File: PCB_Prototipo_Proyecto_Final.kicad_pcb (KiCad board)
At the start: 2 copper layers, 165.1 x 154.9 mm, 107 parts, among them IC1 MCP6486T-E_OT, J1 VIN, J10 Terminal_Sensores_Nivel, J11 Terminal_Sensor_Flujo, J12 Rele_4, J13 Rele_7, J14 Rele_1, J15 Rele_5, J16 Rele_2, J17 Rele_3, J18 Rele_6, J2 Conn_01x15, J3 Conn_01x15, J4 Terminal_Sensor_pH, J5 Terminal_Sensor_Temp_Sumerg, J6 Terminal_Sensor_TDS, J7 Terminal_Sensor_Temp_Sumerg, J8 Terminal_Sensor_Iluminacion, J9 Terminal_Sensor_Temp_y_Hum, K1 SRD-05VDC-SL-C, K2 SRD-05VDC-SL-C, K3 SRD-05VDC-SL-C, K4 SRD-05VDC-SL-C, K5 SRD-05VDC-SL-C, K6 SRD-05VDC-SL-C, K7 SRD-05VDC-SL-C, Q1 PMBT3904,235, Q2 PMBT3904,235, Q3 PMBT3904,235, Q4 PMBT3904,235, Q5 PMBT3904,235, Q6 PMBT3904,235, Q7 PMBT3904,235, U1 LM2596S-5, U2 LM1117-3.3, U3 NXB0108PW-Q100J, U4 MCP23008-xSS

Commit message: Cambios en SCH y PCB.
Se cambio el adaptador de nivel 5-3,3V por un circuito con MOSFET 2N7002, dado que ya no hay stock del NXB. Se modificó el footprint del expansor I/O por uno thorugh-hole.
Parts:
- removed the C19 at (179.2, 156.3)
- removed the C20 at (179.2, 159.3)
- removed C21: 10 uF, 10V, Capacitor_SMD:C_0805_2012Metric
- removed C22: 100 nF, 50V, Capacitor_SMD:C_0805_2012Metric
- removed U4: MCP23008-xSS, Package_SO:SSOP-20_5.3x7.2mm_P0.65mm
- added Q1: 2N7002, Package_TO_SOT_SMD:SOT-23, F.Cu at (163.2, 122.3)
- added Q2: 2N7002, Package_TO_SOT_SMD:SOT-23, F.Cu at (153.3, 186.1)
- added Q3: 2N7002, Package_TO_SOT_SMD:SOT-23, F.Cu at (168.2, 186.0)
- added Q4: 2N7002, Package_TO_SOT_SMD:SOT-23, F.Cu at (183.2, 185.8)
- added Q5: 2N7002, Package_TO_SOT_SMD:SOT-23, F.Cu at (198.3, 185.9)
- added Q6: 2N7002, Package_TO_SOT_SMD:SOT-23, F.Cu at (213.6, 186.1)
- added Q7: 2N7002, Package_TO_SOT_SMD:SOT-23, F.Cu at (161.7, 161.9)
- added Q8: 2N7002, Package_TO_SOT_SMD:SOT-23, F.Cu at (161.2, 143.3)
- added R25: 10K, 1/2W, Resistor_SMD:R_0805_2012Metric, F.Cu at (156.8, 122.4)
- added R26: 10K, 1/2W, Resistor_SMD:R_0805_2012Metric, F.Cu at (163.2, 117.2)
- added R27: 10K, 1/2W, Resistor_SMD:R_0805_2012Metric, F.Cu at (153.3, 191.8)
- added R28: 10K, 1/2W, Resistor_SMD:R_0805_2012Metric, F.Cu at (153.1, 181.0)
- added R29: 10K, 1/2W, Resistor_SMD:R_0805_2012Metric, F.Cu at (168.3, 191.8)
- added R30: 10K, 1/2W, Resistor_SMD:R_0805_2012Metric, F.Cu at (168.2, 180.8)
- added R31: 10K, 1/2W, Resistor_SMD:R_0805_2012Metric, F.Cu at (183.2, 191.6)
- added R32: 10K, 1/2W, Resistor_SMD:R_0805_2012Metric, F.Cu at (183.1, 180.6)
- added R33: 10K, 1/2W, Resistor_SMD:R_0805_2012Metric, F.Cu at (198.2, 191.6)
- added R34: 10K, 1/2W, Resistor_SMD:R_0805_2012Metric, F.Cu at (198.2, 180.4)
- added R35: 10K, 1/2W, Resistor_SMD:R_0805_2012Metric, F.Cu at (213.4, 191.5)
- added R36: 10K, 1/2W, Resistor_SMD:R_0805_2012Metric, F.Cu at (213.6, 180.3)
- added R37: 10K, 1/2W, Resistor_SMD:R_0805_2012Metric, F.Cu at (156.0, 160.9)
- added R38: 10K, 1/2W, Resistor_SMD:R_0805_2012Metric, F.Cu at (161.8, 157.4)
- added R39: 10K, 1/2W, Resistor_SMD:R_0805_2012Metric, F.Cu at (155.6, 143.2)
- added R40: 10K, 1/2W, Resistor_SMD:R_0805_2012Metric, F.Cu at (161.2, 139.0)
- J5: value Terminal_Sensor_Temp_Sumerg -> Terminal_Sensor_CO2
- U3: value NXB0108PW-Q100J -> MCP23008-xP; footprint Package_SO:TSSOP-20_4.4x6.5mm_P0.65mm -> Package_DIP:DIP-18_W7.62mm
- moved R7 336.8 mm to (158.3, 183.3), turned to 90 degrees
- moved R23 332.4 mm to (155.7, 148.5)
- moved C1 329.2 mm to (159.1, 187.9)
- moved R6 321.2 mm to (158.2, 191.8), turned to 90 degrees
- moved R16 320.3 mm to (156.1, 166.3)
- moved C2 319.0 mm to (174.0, 187.4)
- moved R10 318.5 mm to (188.2, 191.7), turned to 90 degrees
- moved R9 316.7 mm to (173.0, 183.1), turned to 90 degrees
- moved C6 315.4 mm to (161.7, 167.3), turned to -90 degrees
- moved C11 315.0 mm to (161.2, 149.4), turned to -90 degrees
- moved R8 307.2 mm to (173.1, 191.7), turned to 90 degrees
- moved R11 301.2 mm to (188.2, 183.0), turned to 90 degrees
- moved C3 293.4 mm to (189.1, 187.2)
- moved R12 287.9 mm to (203.3, 191.6), turned to 90 degrees
- moved C4 284.6 mm to (204.3, 187.1)
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- renumbered C23 to C19, C24 to C20, Q2 to Q10, Q3 to Q11, Q4 to Q12, Q5 to Q13, Q6 to Q14, Q7 to Q15, Q1 to Q9, R25 to R41, R26 to R42, R27 to R43, R28 to R44, R29 to R45, R30 to R46, R31 to R47, R32 to R48, R33 to R49
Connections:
- J2 pad 11: /Microcontrolador/SensorNivel_2 -> /Microcontrolador/SensorNivel_4
- J2 pad 12: /Microcontrolador/SensorNivel_1 -> /Microcontrolador/SensorNivel_5
- J2 pad 13: /Microcontrolador/NXB0108_OE -> unconnected-(J2-Pad13)
- J2 pad 3: /Entradas/TDS_Analog -> unconnected-(J2-Pad3)
- J2 pad 4: /Entradas/Ilum_Analog -> unconnected-(J2-Pad4)
- J2 pad 8: /Microcontrolador/SensorNivel_5 -> /Microcontrolador/SensorNivel_1
- J2 pad 9: /Microcontrolador/SensorNivel_4 -> /Microcontrolador/SensorNivel_2
- J3 pad 12: unconnected-(J3-Pad12) -> /Entradas/TDS_Analog
- J3 pad 13: unconnected-(J3-Pad13) -> /Entradas/Ilum_Analog
- J3 pad 15: unconnected-(J3-Pad15) -> +3.3V
- U3 pad 1: /Microcontrolador/SensorFlujo -> /Microcontrolador/MCP23008_SCL
- U3 pad 10: /Microcontrolador/NXB0108_OE -> /Microcontrolador/Rele_7
- U3 pad 11: GND -> /Microcontrolador/Rele_6
- U3 pad 12: /Entradas/Trigger_pH -> /Microcontrolador/Rele_5
- U3 pad 13: /Entradas/Data_SensorNivel_1 -> /Microcontrolador/Rele_4
- U3 pad 14: /Entradas/Data_SensorNivel_2 -> /Microcontrolador/Rele_3
- U3 pad 15: /Entradas/Data_SensorNivel_3 -> /Microcontrolador/Rele_2
- U3 pad 16: /Entradas/Data_SensorNivel_4 -> /Microcontrolador/Rele_1
- U3 pad 17: /Entradas/Data_SensorNivel_5 -> /Microcontrolador/Trigger__pH
- U3 pad 18: /Entradas/Data_SensorCO2 -> +3.3V
- U3 pad 2: +3.3V -> /Microcontrolador/MCP23008_SDA
- U3 pad 3: /Microcontrolador/SensorCO2 -> GND
- U3 pad 4: /Microcontrolador/SensorNivel_5 -> GND
- U3 pad 5: /Microcontrolador/SensorNivel_4 -> GND
- U3 pad 6: /Microcontrolador/SensorNivel_3 -> /Microcontrolador/MCP23008_RESET
- U3 pad 7: /Microcontrolador/SensorNivel_2 -> unconnected-(U3-Pad7)
- U3 pad 8: /Microcontrolador/SensorNivel_1 -> unconnected-(U3-Pad8)
- U3 pad 9: /Microcontrolador/Trigger__pH -> GND

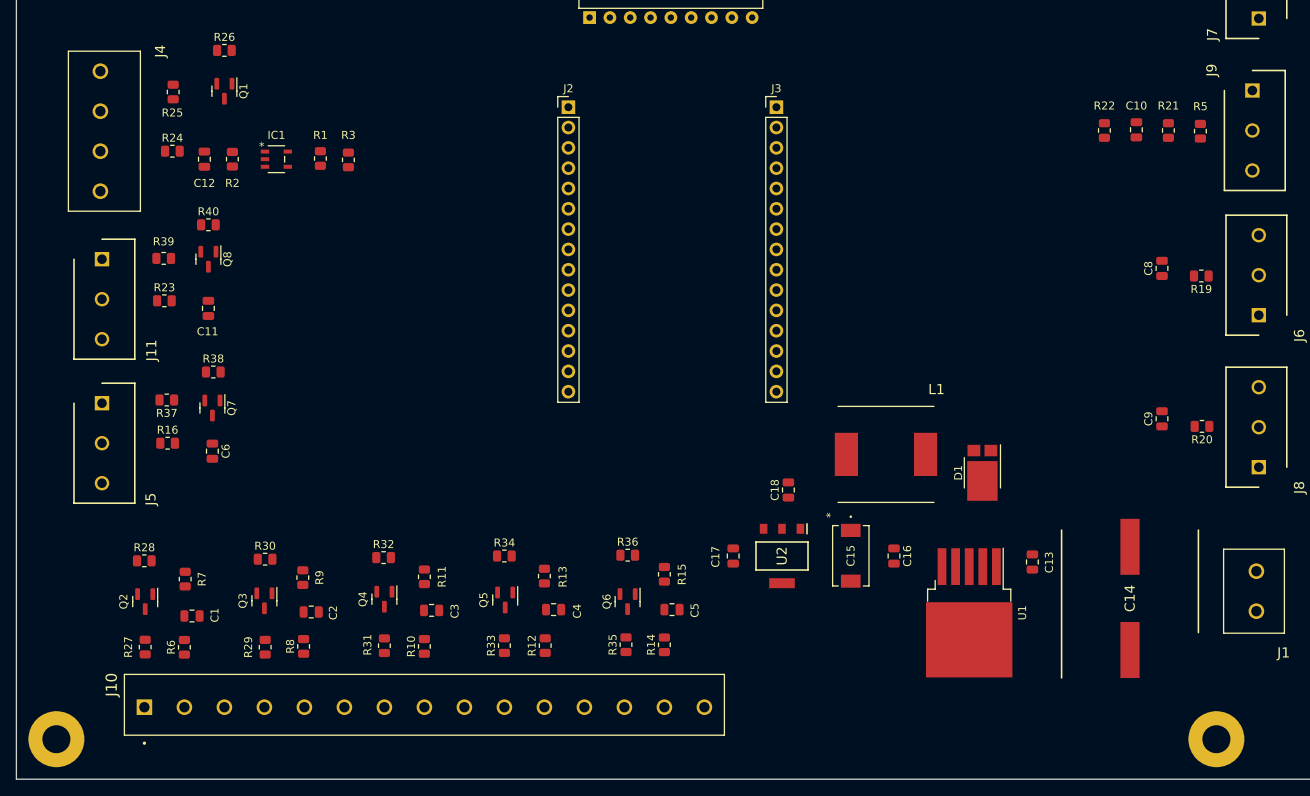
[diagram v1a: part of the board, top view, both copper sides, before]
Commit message: Continuación de trazado de PCB.
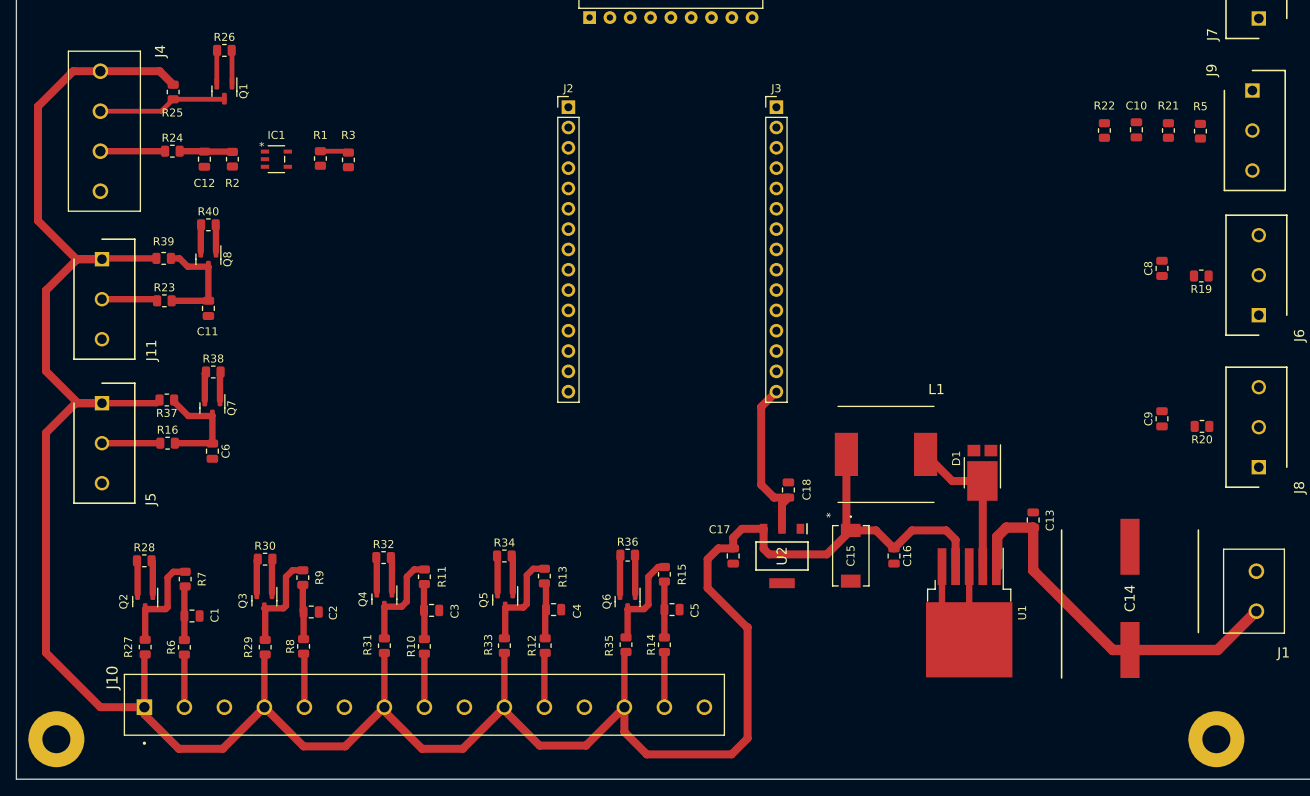
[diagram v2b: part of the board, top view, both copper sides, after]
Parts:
- moved C13 5.25 mm to (264.3, 175.9)
- turned R33 to -90 degrees
- turned R35 to -90 degrees
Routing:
- net +5V: track 0.00 -> 345.8 mm
- net +3.3V: track 0.00 -> 54.2 mm
- net /Fuentes/VIN_24V: track 0.00 -> 48.1 mm
- net GND: track 0.00 -> 19.7 mm
- net Net-(D1-Pad3): track 0.00 -> 19.2 mm
- net /Entradas/Trigger_pH: track 0.00 -> 16.1 mm
- net /Entradas/Data_SensorCO2: track 0.00 -> 14.0 mm
- net /Entradas/Data_SensorFlujo: track 0.00 -> 14.0 mm
- net /Entradas/Data_SensorNivel_1: track 0.00 -> 12.9 mm
- net /Entradas/Data_SensorNivel_4: track 0.00 -> 12.9 mm
- net /Entradas/Data_SensorNivel_2: track 0.00 -> 12.9 mm
- net /Entradas/Data_SensorNivel_3: track 0.00 -> 12.7 mm
- net /Entradas/Data_SensorNivel_5: track 0.00 -> 12.5 mm
- net /Entradas/SensorpH: track 0.00 -> 8.09 mm
- net /Entradas/SensorCO2: track 0.00 -> 7.29 mm
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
